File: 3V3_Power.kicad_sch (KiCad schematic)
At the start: 3 parts

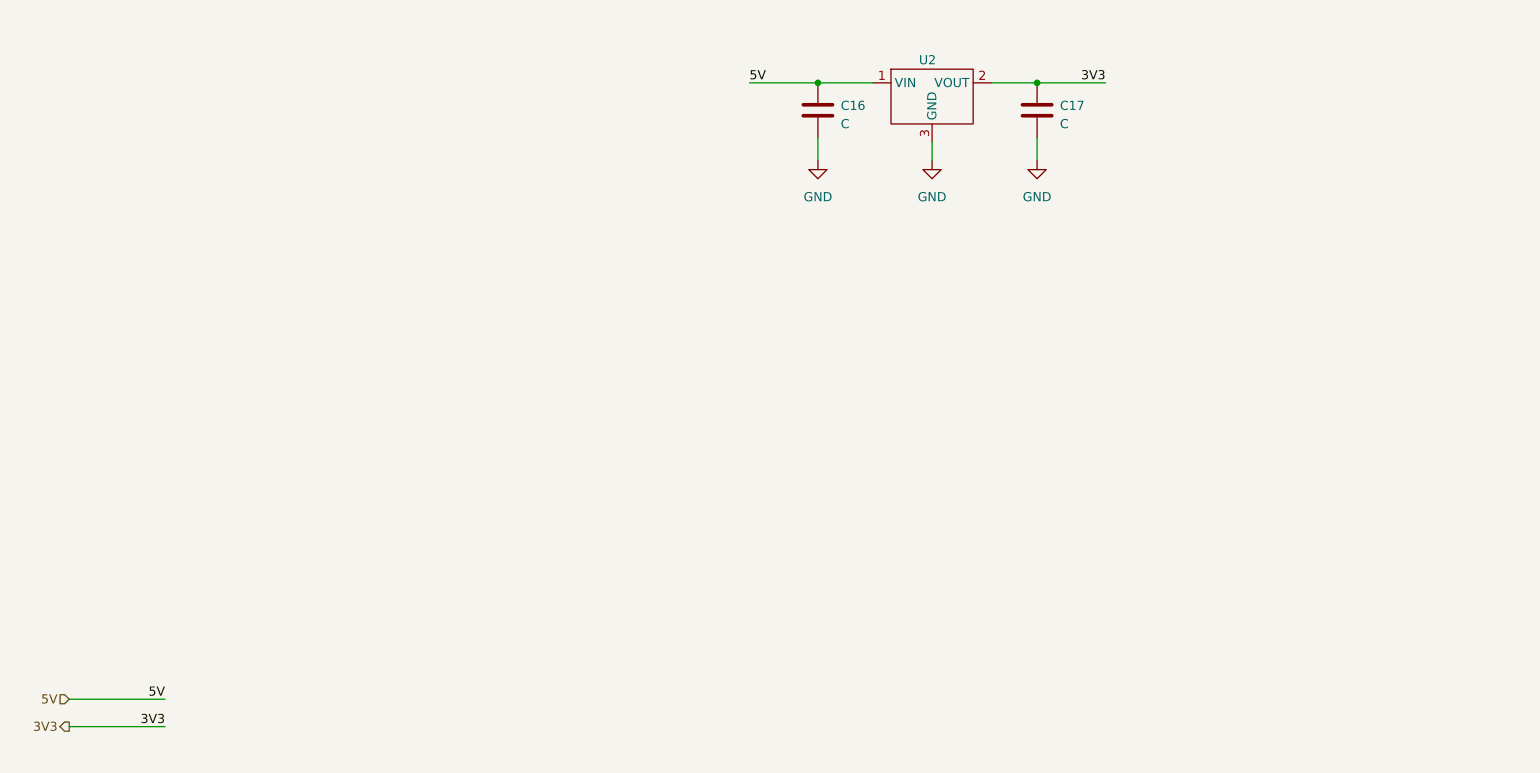
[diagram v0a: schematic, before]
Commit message: Added RS-485 Transceiver
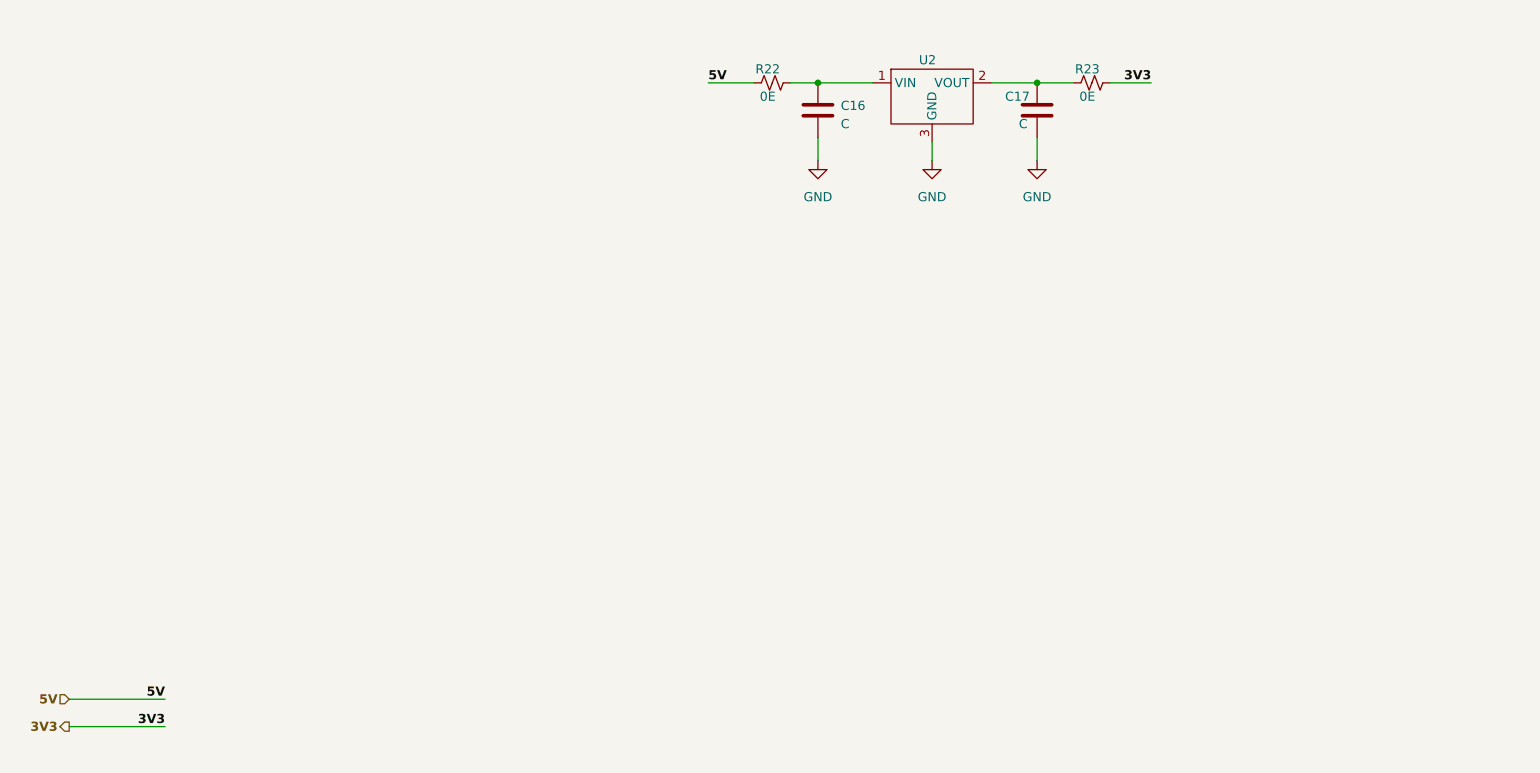
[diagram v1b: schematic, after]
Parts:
- added R22, R23: 0E, symbol ESP32-S3_DB:R_Small_US
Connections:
- net 3V3: now also R23.2; no longer C17.1, U2.2 (VOUT)
- net 5V: now also R22.1; no longer C16.1, U2.1 (VIN)
- new net: C16.1, R22.2, U2.1 (VIN)
- new net: C17.1, R23.1, U2.2 (VOUT)
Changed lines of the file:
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@@
   (junction (at 161.925 89.535) (diameter 0) (color 0 0 0 0)
   )
-  (wire (pts (xy 161.925 89.535) (xy 171.45 89.535))
+  (wire (pts (xy 161.925 89.535) (xy 167.005 89.535))
+    (stroke (width 0) (type default))
+  )
+  (wire (pts (xy 172.085 89.535) (xy 177.8 89.535))
     (stroke (width 0) (type default))
   )
@@
     (stroke (width 0) (type default))
   )
-  (wire (pts (xy 121.92 89.535) (xy 131.445 89.535))
+  (wire (pts (xy 116.205 89.535) (xy 122.555 89.535))
     (stroke (width 0) (type default))
   )
@@
     (stroke (width 0) (type default))
   )
+  (wire (pts (xy 127.635 89.535) (xy 131.445 89.535))
+    (stroke (width 0) (type default))
+  )
   (wire (pts (xy 40.64 175.26) (xy 27.305 175.26))
     (stroke (width 0) (type default))
@@
   )
   (label "5V" (at 40.64 175.26 180) (fields_autoplaced)
-    (effects (font (size 1.27 1.27)) (justify right bottom))
+    (effects (font (size 1.27 1.27) (thickness 0.254) bold (color 255 0 0 1)) (justify right bottom))
   )
   (label "3V3" (at 40.64 179.07 180) (fields_autoplaced)
-    (effects (font (size 1.27 1.27)) (justify right bottom))
-  )
-  (label "3V3" (at 171.45 89.535 180) (fields_autoplaced)
-    (effects (font (size 1.27 1.27)) (justify right bottom))
-  )
-  (label "5V" (at 121.92 89.535 0) (fields_autoplaced)
-    (effects (font (size 1.27 1.27)) (justify left bottom))
+    (effects (font (size 1.27 1.27) (thickness 0.254) bold (color 255 0 0 1)) (justify right bottom))
+  )
+  (label "3V3" (at 177.8 89.535 180) (fields_autoplaced)
+    (effects (font (size 1.27 1.27) (thickness 0.254) bold (color 255 0 0 1)) (justify right bottom))
+  )
+  (label "5V" (at 116.205 89.535 0) (fields_autoplaced)
+    (effects (font (size 1.27 1.27) (thickness 0.254) bold (color 255 0 0 1)) (justify left bottom))
   )
   (hierarchical_label "3V3" (shape output) (at 27.305 179.07 180) (fields_autoplaced)
-    (effects (font (size 1.27 1.27)) (justify right))
+    (effects (font (size 1.27 1.27) (thickness 0.254) bold (color 255 0 0 1)) (justify right))
   )
   (hierarchical_label "5V" (shape input) (at 27.305 175.26 180) (fields_autoplaced)
-    (effects (font (size 1.27 1.27)) (justify right))
+    (effects (font (size 1.27 1.27) (thickness 0.254) bold (color 255 0 0 1)) (justify right))
   )
   (symbol (lib_id "ESP32-S3_DB:GND") (at 161.925 100.33 0) (unit 1)
@@
     )
   )
+  (symbol (lib_id "ESP32-S3_DB:R_Small_US") (at 125.095 89.535 90) (unit 1)
+    (in_bom yes) (on_board yes) (dnp no)
+    (property "Reference" "R22" (at 124.46 87.63 90)
+      (effects (font (size 1.27 1.27)))
+    )
+    (property "Value" "0E" (at 124.46 91.44 90)
+      (effects (font (size 1.27 1.27)))
+    )
+    (property "Footprint" "" (at 125.095 89.535 0)
+      (effects (font (size 1.27 1.27)) hide)
+    )
+    (property "Datasheet" "~" (at 125.095 89.535 0)
+      (effects (font (size 1.27 1.27)) hide)
+    )
+    (pin "1")
+    (pin "2")
+    (instances
+      (project "ESP32-S3_DB"
+        (path "/b7fc4bd3-c219-4455-832b-8d795385dcf1/efdd6c4f-0b42-4473-ae3b-b7dbb76b2e75"
+          (reference "R22") (unit 1)
+        )
+      )
+    )
+  )
   (symbol (lib_id "ESP32-S3_DB:C") (at 161.925 93.345 0) (unit 1)
-    (in_bom yes) (on_board yes) (dnp no) (fields_autoplaced)
-    (property "Reference" "C17" (at 165.1 92.71 0)
-      (effects (font (size 1.27 1.27)) (justify left))
-    )
-    (property "Value" "C" (at 165.1 95.25 0)
+    (in_bom yes) (on_board yes) (dnp no)
+    (property "Reference" "C17" (at 157.48 91.44 0)
+      (effects (font (size 1.27 1.27)) (justify left))
+    )
+    (property "Value" "C" (at 159.385 95.25 0)
       (effects (font (size 1.27 1.27)) (justify left))
     )
@@
         )
       )
+    )
+  )
+  (symbol (lib_id "ESP32-S3_DB:R_Small_US") (at 169.545 89.535 90) (unit 1)
+    (in_bom yes) (on_board yes) (dnp no)
+    (property "Reference" "R23" (at 168.91 87.63 90)
+      (effects (font (size 1.27 1.27)))
+    )
+    (property "Value" "0E" (at 168.91 91.44 90)
+      (effects (font (size 1.27 1.27)))
+    )
+    (property "Footprint" "" (at 169.545 89.535 0)
+      (effects (font (size 1.27 1.27)) hide)
+    )
+    (property "Datasheet" "~" (at 169.545 89.535 0)
+      (effects (font (size 1.27 1.27)) hide)
+    )
+    (pin "1")
+    (pin "2")
+    (instances
+      (project "ESP32-S3_DB"
+        (path "/b7fc4bd3-c219-4455-832b-8d795385dcf1/efdd6c4f-0b42-4473-ae3b-b7dbb76b2e75"
+          (reference "R23") (unit 1)
+        )
+      )

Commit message: Added Female Headers
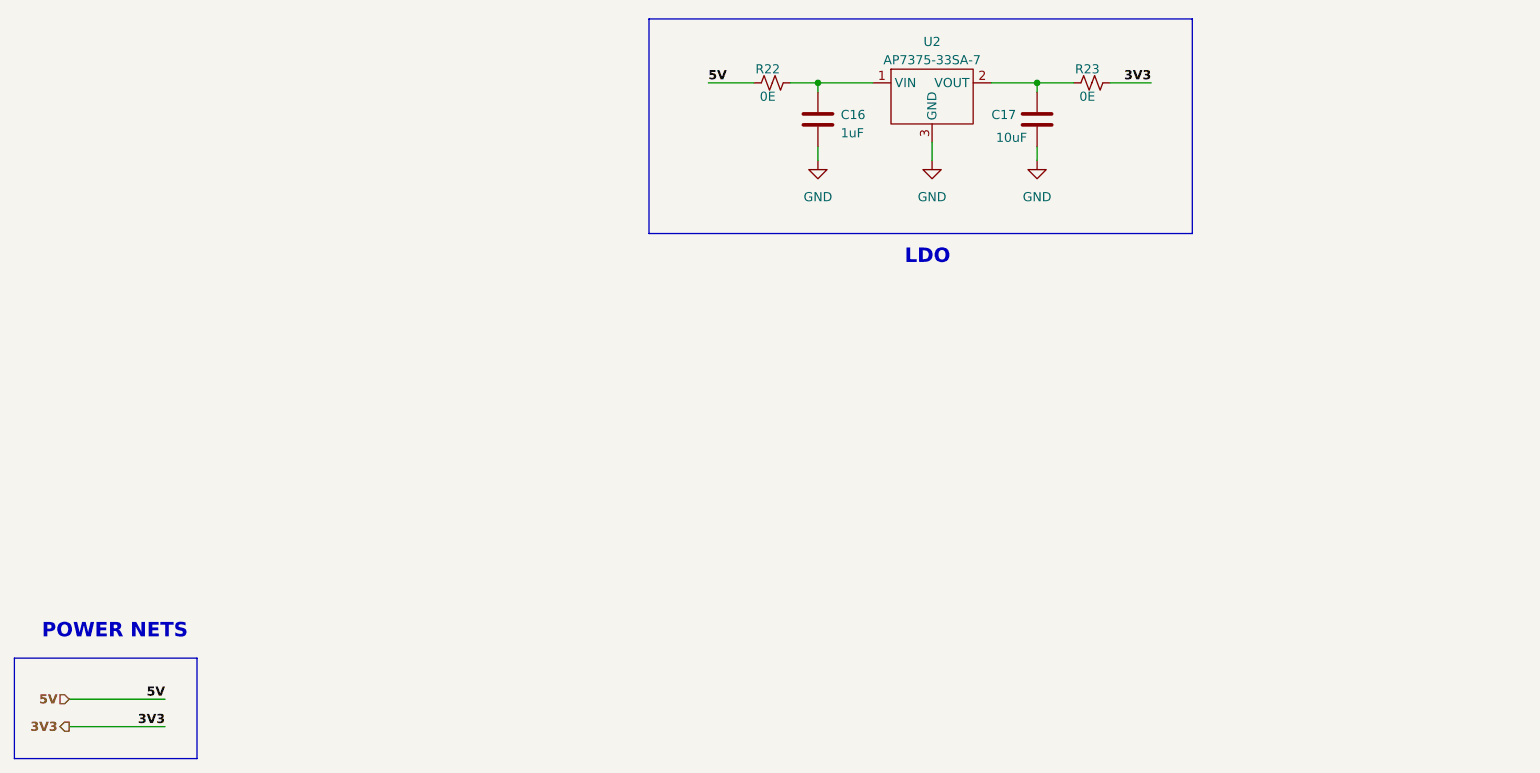
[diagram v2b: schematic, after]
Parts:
- C16: value C -> 1uF
- C17: value C -> 10uF
- U2: value ~ -> AP7375-33SA-7
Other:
- note added: "LDO"
- note added: "POWER NETS"
- moved on the sheet: C16, C17
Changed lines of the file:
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@@
     (stroke (width 0) (type default))
   )
-  (wire (pts (xy 27.305 179.07) (xy 40.64 179.07))
+  (wire (pts (xy 161.925 90.805) (xy 161.925 89.535))
     (stroke (width 0) (type default))
   )
-  (wire (pts (xy 161.925 100.33) (xy 161.925 97.155))
+  (bus (pts (xy 45.085 169.545) (xy 45.085 183.515))
+    (stroke (width 1) (type default) (color 72 72 72 1))
+  )
+  (wire (pts (xy 27.305 179.07) (xy 40.64 179.07))
+    (stroke (width 0.5) (type default) (color 255 0 0 1))
+  )
+  (wire (pts (xy 161.925 100.33) (xy 161.925 98.425))
     (stroke (width 0) (type default))
   )
@@
     (stroke (width 0) (type default))
   )
-  (wire (pts (xy 131.445 100.33) (xy 131.445 97.155))
+  (bus (pts (xy 107.95 80.645) (xy 107.95 110.49))
+    (stroke (width 1) (type default) (color 72 72 72 1))
+  )
+  (bus (pts (xy 183.515 80.645) (xy 183.515 110.49))
+    (stroke (width 1) (type default) (color 72 72 72 1))
+  )
+  (wire (pts (xy 131.445 100.33) (xy 131.445 98.425))
     (stroke (width 0) (type default))
+  )
+  (bus (pts (xy 45.085 183.515) (xy 19.685 183.515))
+    (stroke (width 1) (type default) (color 72 72 72 1))
+  )
+  (bus (pts (xy 183.515 110.49) (xy 107.95 110.49))
+    (stroke (width 1) (type default) (color 72 72 72 1))
+  )
+  (bus (pts (xy 107.95 80.645) (xy 183.515 80.645))
+    (stroke (width 1) (type default) (color 72 72 72 1))
   )
   (wire (pts (xy 147.32 100.33) (xy 147.32 97.79))
@@
   )
   (wire (pts (xy 40.64 175.26) (xy 27.305 175.26))
-    (stroke (width 0) (type default))
+    (stroke (width 0.5) (type default) (color 255 0 0 1))
   )
   (wire (pts (xy 131.445 89.535) (xy 139.065 89.535))
     (stroke (width 0) (type default))
+  )
+  (bus (pts (xy 19.685 169.545) (xy 19.685 183.515))
+    (stroke (width 1) (type default) (color 72 72 72 1))
+  )
+  (wire (pts (xy 131.445 90.805) (xy 131.445 89.535))
+    (stroke (width 0) (type default))
+  )
+  (bus (pts (xy 19.685 169.545) (xy 45.085 169.545))
+    (stroke (width 1) (type default) (color 72 72 72 1))
+  )
+  (text "POWER NETS" (at 23.495 167.005 0)
+    (effects (font (size 2 2) bold (color 255 0 0 1)) (justify left bottom))
+  )
+  (text "LDO" (at 143.51 114.935 0)
+    (effects (font (size 2 2) bold (color 255 0 0 1)) (justify left bottom))
   )
   (label "5V" (at 40.64 175.26 180) (fields_autoplaced)
@@
   )
   (symbol (lib_id "ESP32-S3_DB:AP7375-33SA-7") (at 146.685 86.36 0) (unit 1)
-    (in_bom yes) (on_board yes) (dnp no) (fields_autoplaced)
-    (property "Reference" "U2" (at 146.685 86.36 0)
+    (in_bom yes) (on_board yes) (dnp no)
+    (property "Reference" "U2" (at 147.32 83.82 0)
       (effects (font (size 1.27 1.27)))
     )
-    (property "Value" "~" (at 146.685 86.36 0)
+    (property "Value" "AP7375-33SA-7" (at 147.32 86.36 0)
       (effects (font (size 1.27 1.27)))
     )
@@
     )
   )
-  (symbol (lib_id "ESP32-S3_DB:C") (at 131.445 93.345 0) (unit 1)
+  (symbol (lib_id "ESP32-S3_DB:C") (at 131.445 94.615 0) (unit 1)
     (in_bom yes) (on_board yes) (dnp no) (fields_autoplaced)
-    (property "Reference" "C16" (at 134.62 92.71 0)
+    (property "Reference" "C16" (at 134.62 93.98 0)
       (effects (font (size 1.27 1.27)) (justify left))
     )
-    (property "Value" "C" (at 134.62 95.25 0)
+    (property "Value" "1uF" (at 134.62 96.52 0)
       (effects (font (size 1.27 1.27)) (justify left))
     )
-    (property "Footprint" "" (at 132.4102 97.155 0)
+    (property "Footprint" "" (at 132.4102 98.425 0)
       (effects (font (size 1.27 1.27)) hide)
     )
-    (property "Datasheet" "~" (at 131.445 93.345 0)
+    (property "Datasheet" "~" (at 131.445 94.615 0)
       (effects (font (size 1.27 1.27)) hide)
     )
@@
     )
   )
-  (symbol (lib_id "ESP32-S3_DB:C") (at 161.925 93.345 0) (unit 1)
+  (symbol (lib_id "ESP32-S3_DB:C") (at 161.925 94.615 0) (unit 1)
     (in_bom yes) (on_board yes) (dnp no)
-    (property "Reference" "C17" (at 157.48 91.44 0)
+    (property "Reference" "C17" (at 155.575 93.98 0)
       (effects (font (size 1.27 1.27)) (justify left))
     )
-    (property "Value" "C" (at 159.385 95.25 0)
+    (property "Value" "10uF" (at 156.21 97.155 0)
       (effects (font (size 1.27 1.27)) (justify left))
     )
-    (property "Footprint" "" (at 162.8902 97.155 0)
+    (property "Footprint" "" (at 162.8902 98.425 0)
       (effects (font (size 1.27 1.27)) hide)
     )
-    (property "Datasheet" "~" (at 161.925 93.345 0)
+    (property "Datasheet" "~" (at 161.925 94.615 0)
       (effects (font (size 1.27 1.27)) hide)
     )

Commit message: Assigned PN and Footprint for C
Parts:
- C16: footprint (none) -> ESP32-S3_DB:C_0603_1608Metric; PN (none) -> CC0603KRX5R8BB105
- C17: footprint (none) -> ESP32-S3_DB:C_0805_2012Metric; PN (none) -> CL21A106KAYNNNE
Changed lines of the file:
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@@
       (effects (font (size 1.27 1.27)) (justify left))
     )
-    (property "Footprint" "" (at 132.4102 98.425 0)
+    (property "Footprint" "ESP32-S3_DB:C_0603_1608Metric" (at 132.4102 98.425 0)
       (effects (font (size 1.27 1.27)) hide)
     )
     (property "Datasheet" "~" (at 131.445 94.615 0)
+      (effects (font (size 1.27 1.27)) hide)
+    )
+    (property "PN" "CC0603KRX5R8BB105" (at 131.445 94.615 0)
       (effects (font (size 1.27 1.27)) hide)
     )
@@
       (effects (font (size 1.27 1.27)) (justify left))
     )
-    (property "Footprint" "" (at 162.8902 98.425 0)
+    (property "Footprint" "ESP32-S3_DB:C_0805_2012Metric" (at 162.8902 98.425 0)
       (effects (font (size 1.27 1.27)) hide)
     )
@@
       (effects (font (size 1.27 1.27)) hide)
     )
+    (property "PN" "CL21A106KAYNNNE" (at 161.925 94.615 0)
+      (effects (font (size 1.27 1.27)) hide)
+    )

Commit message: Assigned footprints
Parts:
- C16: footprint ESP32-S3_DB:C_0603_1608Metric -> ESP32-S3_Dev_Board:C_0603_1608Metric
- C17: footprint ESP32-S3_DB:C_0805_2012Metric -> ESP32-S3_Dev_Board:C_0805_2012Metric
- R22, R23: footprint (none) -> ESP32-S3_Dev_Board:R_0603_1608Metric; PN (none) -> RC0603JR-070RL
- U2: footprint (none) -> ESP32-S3_Dev_Board:SOT-23-3; PN (none) -> AP7375-33SA-7
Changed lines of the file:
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@@
       (effects (font (size 1.27 1.27)))
     )
-    (property "Footprint" "" (at 146.685 86.36 0)
+    (property "Footprint" "ESP32-S3_Dev_Board:SOT-23-3" (at 146.685 86.36 0)
       (effects (font (size 1.27 1.27)) hide)
     )
     (property "Datasheet" "" (at 146.685 86.36 0)
+      (effects (font (size 1.27 1.27)) hide)
+    )
+    (property "PN" "AP7375-33SA-7" (at 146.685 86.36 0)
       (effects (font (size 1.27 1.27)) hide)
     )
@@
       (effects (font (size 1.27 1.27)) (justify left))
     )
-    (property "Footprint" "ESP32-S3_DB:C_0603_1608Metric" (at 132.4102 98.425 0)
+    (property "Footprint" "ESP32-S3_Dev_Board:C_0603_1608Metric" (at 132.4102 98.425 0)
       (effects (font (size 1.27 1.27)) hide)
     )
@@
       (effects (font (size 1.27 1.27)))
     )
-    (property "Footprint" "" (at 125.095 89.535 0)
+    (property "Footprint" "ESP32-S3_Dev_Board:R_0603_1608Metric" (at 125.095 89.535 0)
       (effects (font (size 1.27 1.27)) hide)
     )
     (property "Datasheet" "~" (at 125.095 89.535 0)
+      (effects (font (size 1.27 1.27)) hide)
+    )
+    (property "PN" "RC0603JR-070RL" (at 125.095 89.535 0)
       (effects (font (size 1.27 1.27)) hide)
     )
@@
       (effects (font (size 1.27 1.27)) (justify left))
     )
-    (property "Footprint" "ESP32-S3_DB:C_0805_2012Metric" (at 162.8902 98.425 0)
+    (property "Footprint" "ESP32-S3_Dev_Board:C_0805_2012Metric" (at 162.8902 98.425 0)
       (effects (font (size 1.27 1.27)) hide)
     )
@@
       (effects (font (size 1.27 1.27)))
     )
-    (property "Footprint" "" (at 169.545 89.535 0)
+    (property "Footprint" "ESP32-S3_Dev_Board:R_0603_1608Metric" (at 169.545 89.535 0)
       (effects (font (size 1.27 1.27)) hide)
     )
@@
       (effects (font (size 1.27 1.27)) hide)
     )
+    (property "PN" "RC0603JR-070RL" (at 169.545 89.535 0)
+      (effects (font (size 1.27 1.27)) hide)
+    )

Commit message: Instigated PCB Design
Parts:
- removed U2: AP7375-33SA-7, ESP32-S3_Dev_Board:SOT-23-3, symbol ESP32-S3_DB:AP7375-33SA-7
- added U5: AP2127N-3.3TRG1, ESP32-S3_Dev_Board:SOT-23-3, symbol ESP32-S3_DB:AP2127N-3.3TRG1
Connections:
- net GND: now also U5.1 (GND)
- net at C16.1, R22.2: now also U5.3 (VIN)
- net at C17.1, R23.1: now also U5.2 (VOUT)
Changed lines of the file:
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@@
-    )
-  )
-  (symbol (lib_id "ESP32-S3_DB:AP7375-33SA-7") (at 146.685 86.36 0) (unit 1)
-    (in_bom yes) (on_board yes) (dnp no)
-    (property "Reference" "U2" (at 147.32 83.82 0)
-      (effects (font (size 1.27 1.27)))
-    )
-    (property "Value" "AP7375-33SA-7" (at 147.32 86.36 0)
-      (effects (font (size 1.27 1.27)))
-    )
-    (property "Footprint" "ESP32-S3_Dev_Board:SOT-23-3" (at 146.685 86.36 0)
-      (effects (font (size 1.27 1.27)) hide)
-    )
-    (property "Datasheet" "" (at 146.685 86.36 0)
-      (effects (font (size 1.27 1.27)) hide)
-    )
-    (property "PN" "AP7375-33SA-7" (at 146.685 86.36 0)
-      (effects (font (size 1.27 1.27)) hide)
-    )
-    (pin "1")
-    (pin "2")
-    (pin "3")
-    (instances
-      (project "ESP32-S3_DB"
-        (path "/b7fc4bd3-c219-4455-832b-8d795385dcf1/efdd6c4f-0b42-4473-ae3b-b7dbb76b2e75"
-          (reference "U2") (unit 1)
-        )
-      )
     )
   )
@@
         )
       )
+    )
+  )
+  (symbol (lib_id "ESP32-S3_DB:AP2127N-3.3TRG1") (at 146.685 86.36 0) (unit 1)
+    (in_bom yes) (on_board yes) (dnp no) (fields_autoplaced)
+    (property "Reference" "U5" (at 147.32 83.185 0)
+      (effects (font (size 1.27 1.27)))
+    )
+    (property "Value" "AP2127N-3.3TRG1" (at 147.32 85.725 0)
+      (effects (font (size 1.27 1.27)))
+    )
+    (property "Footprint" "ESP32-S3_Dev_Board:SOT-23-3" (at 146.685 86.36 0)
+      (effects (font (size 1.27 1.27)) hide)
+    )
+    (property "Datasheet" "" (at 146.685 86.36 0)
+      (effects (font (size 1.27 1.27)) hide)
+    )
+    (property "PN" "AP2127N-3.3TRG1" (at 146.685 86.36 0)
+      (effects (font (size 1.27 1.27)) hide)
+    )
+    (pin "1")
+    (pin "2")
+    (pin "3")
+    (instances
+      (project "ESP32-S3_DB"
+        (path "/b7fc4bd3-c219-4455-832b-8d795385dcf1/efdd6c4f-0b42-4473-ae3b-b7dbb76b2e75"
+          (reference "U5") (unit 1)
+        )
+      )
